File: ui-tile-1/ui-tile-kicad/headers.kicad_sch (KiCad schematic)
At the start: 2 parts

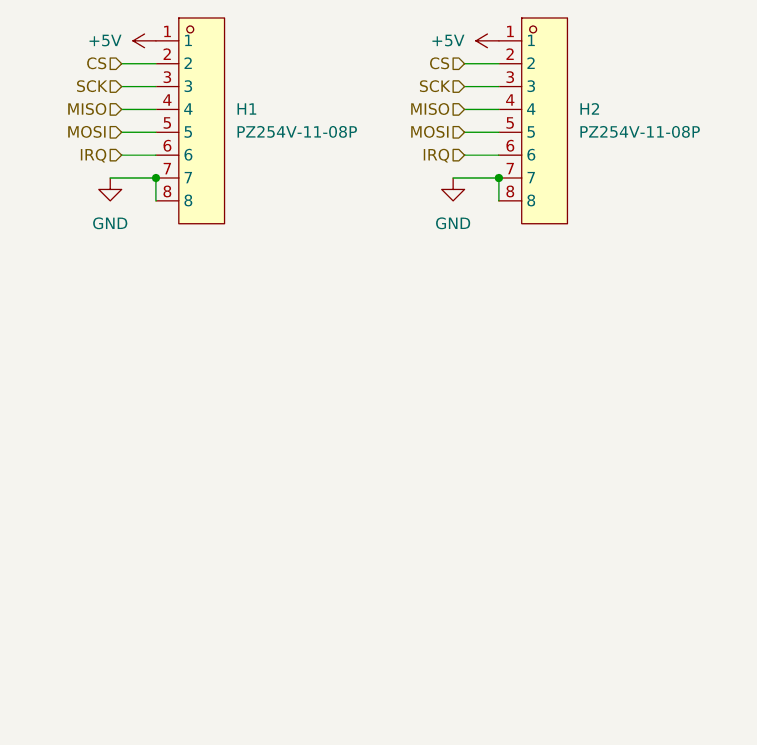
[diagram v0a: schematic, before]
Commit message: added fpc connector
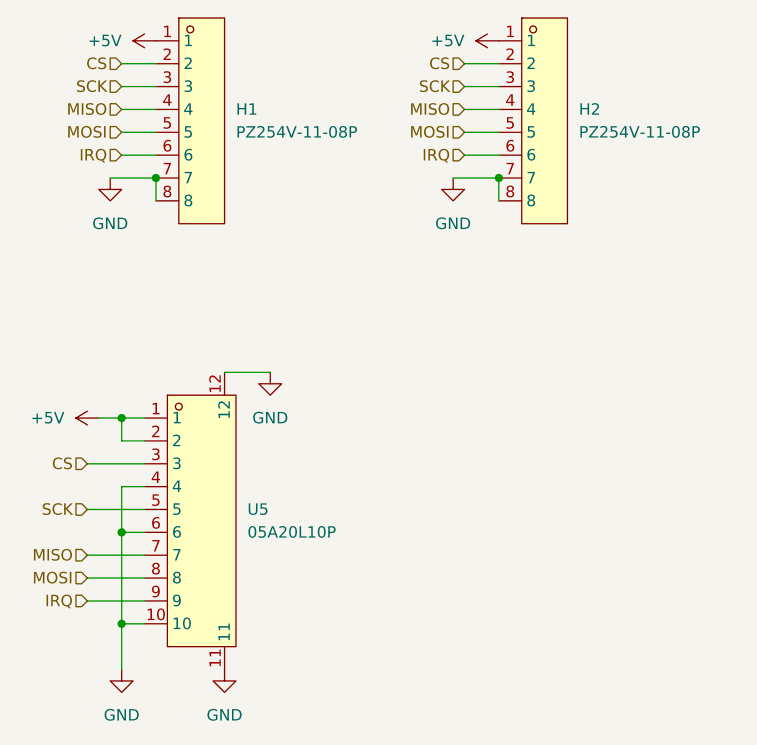
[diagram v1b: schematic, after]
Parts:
- added U5: 05A20L10P, jlcpcb:FPC-SMD_10P-P0.50_05A20L10P, symbol jlcpcb:05A20L10P
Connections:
- net +5V: now also U5.1, U5.2
- net CS: now also U5.3
- net GND: now also U5.10, U5.11, U5.12, U5.4, U5.6
- net IRQ: now also U5.9
- net MISO: now also U5.7
- net MOSI: now also U5.8
- net SCK: now also U5.5
